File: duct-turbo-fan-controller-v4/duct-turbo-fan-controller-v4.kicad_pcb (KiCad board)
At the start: 2 copper layers, 42.7 x 48.8 mm, 45 parts, among them J1 Screw_Terminal_01x04, J2 Conn_01x04, J3 USB_OTG, J4 AudioJack4, J7 Conn_01x04, Q1 MMBT3904, Q2 BSS84, SW1 SW_Push, SW2 SW_Push, U1 SCD41-D-R2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

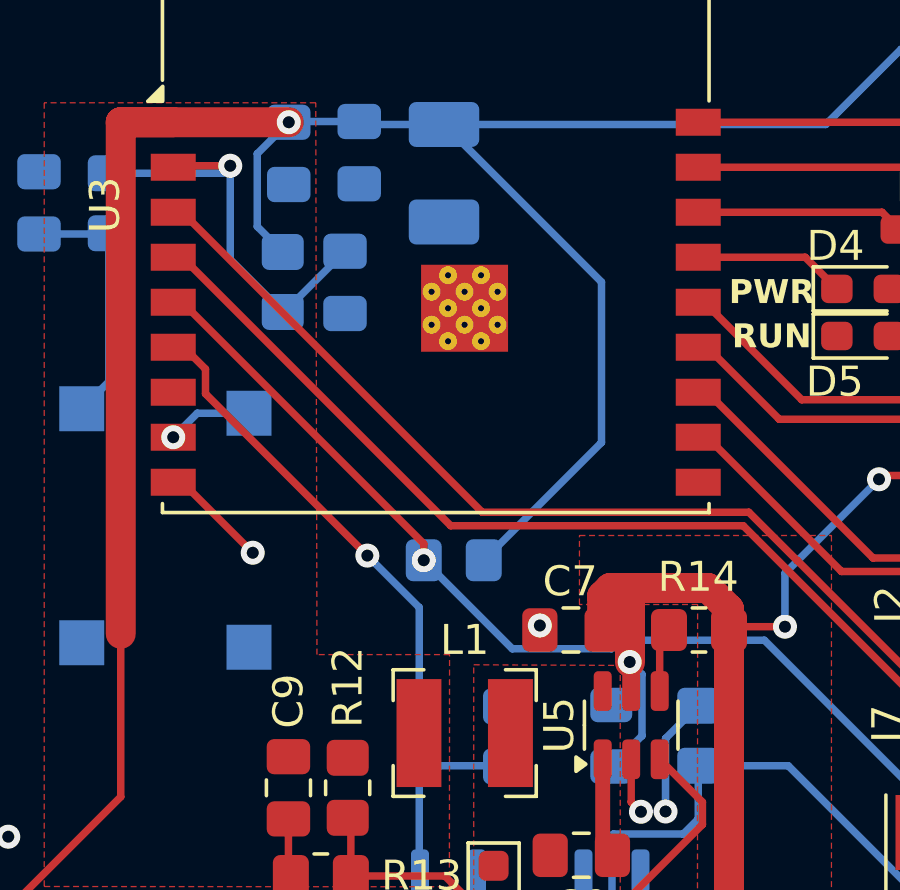
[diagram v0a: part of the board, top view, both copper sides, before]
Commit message: Add gnd tracks where fill zone incomplete.
Update leds in schematic to be more readable.
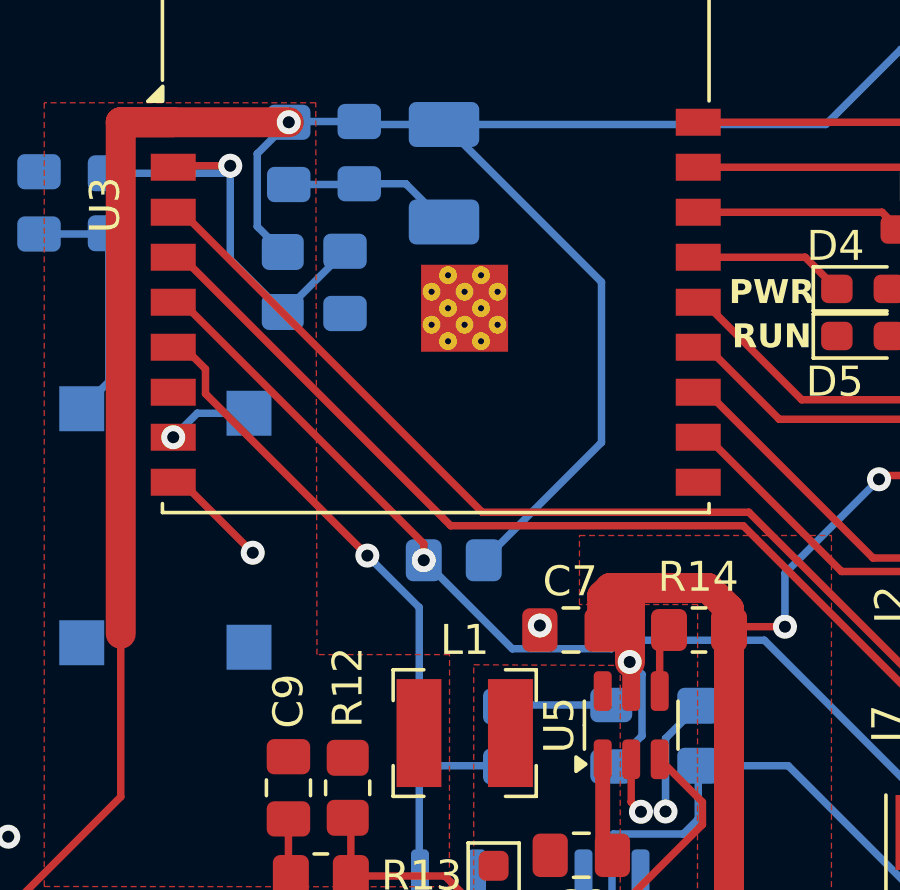
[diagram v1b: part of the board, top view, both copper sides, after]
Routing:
- net GND: track 37.1 -> 46.5 mm
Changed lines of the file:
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@@
+	)
+	(segment
+		(start 87.45 55.375)
+		(end 88.725 56.65)
+		(width 0.25)
+		(layer "B.Cu")
+		(net 2)
 	)
 	(segment
@@
 	)
 	(segment
+		(start 85.9 55.375)
+		(end 87.45 55.375)
+		(width 0.25)
+		(layer "B.Cu")
+		(net 2)
+	)
+	(segment
 		(start 89.825 78.3)
 		(end 89.825 80.055)
@@
 	)
 	(segment
+		(start 90.775 72.75)
+		(end 90.725 72.8)
+		(width 0.25)
+		(layer "B.Cu")
+		(net 2)
+	)
+	(segment
+		(start 83.55 55.4)
+		(end 85.875 55.4)
+		(width 0.25)
+		(layer "B.Cu")
+		(net 2)
+	)
+	(segment
 		(start 110.225 80.9)
 		(end 110.225 80.875)
+		(width 0.25)
+		(layer "B.Cu")
+		(net 2)
+	)
+	(segment
+		(start 85.875 55.4)
+		(end 85.9 55.375)
 		(width 0.25)
 		(layer "B.Cu")
@@
 		(width 0.25)
 		(layer "B.Cu")
+		(net 2)
+	)
+	(segment
+		(start 94.3 72.75)
+		(end 90.775 72.75)
+		(width 0.25)
+		(layer "B.Cu")

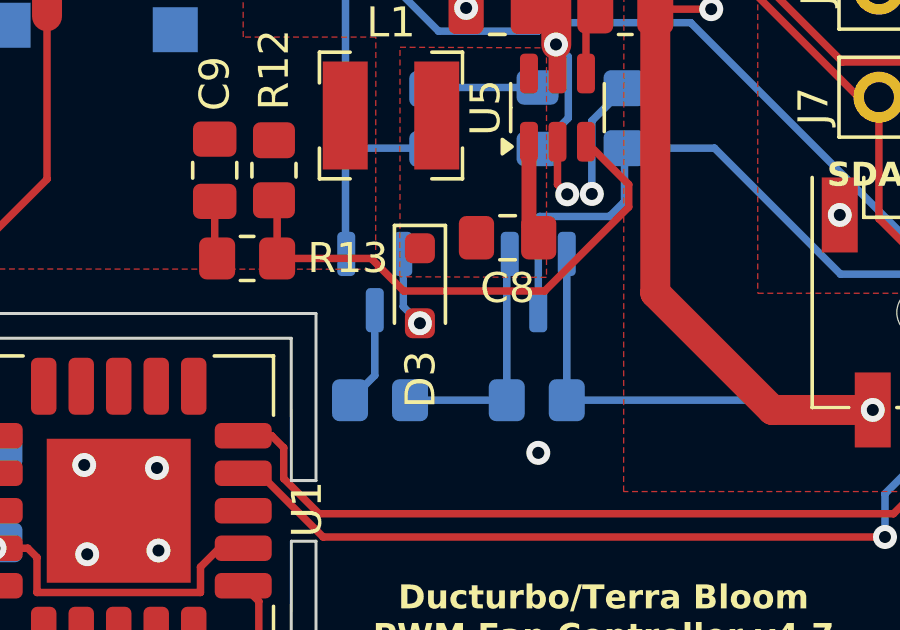
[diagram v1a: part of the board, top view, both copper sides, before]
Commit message: Fix buck diode footprint on pcb
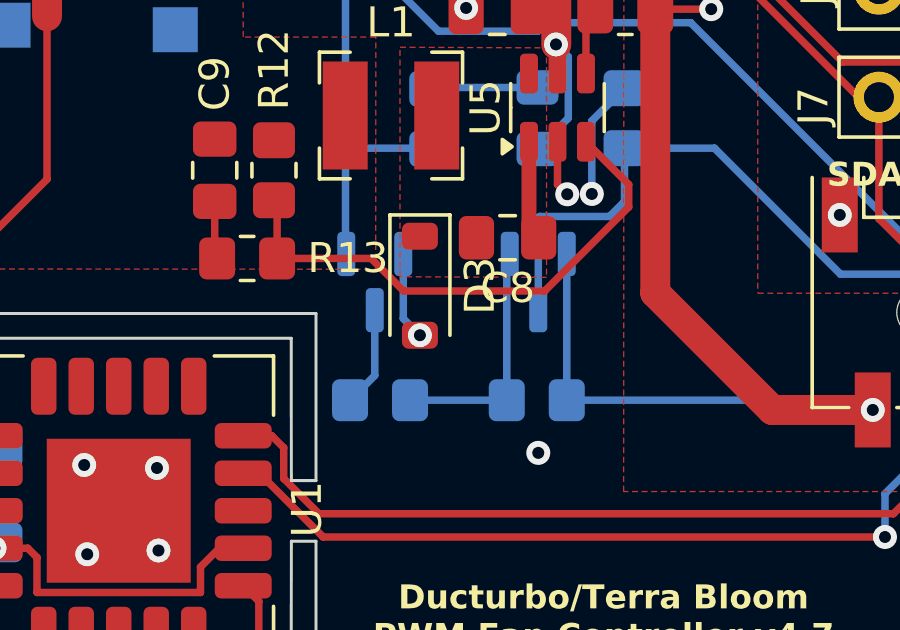
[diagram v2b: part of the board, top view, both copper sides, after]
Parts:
- C7, C9: value C_Small -> 10uF X7R
- C8: value C_Small -> 0.1uF
- D3: footprint Diode_SMD:D_SOD-323_HandSoldering -> Diode_SMD:D_SOD-123
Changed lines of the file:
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@@
 			)
 		)
-		(property "Value" "C_Small"
+		(property "Value" "0.1uF"
 			(at 0 1.68 0)
 			(layer "F.Fab")
@@
 			)
 		)
-		(property "Value" "C_Small"
+		(property "Value" "10uF X7R"
 			(at 0 1.68 90)
 			(layer "F.Fab")
@@
 		)
 	)
-	(footprint "Diode_SMD:D_SOD-323_HandSoldering"
+	(footprint "Diode_SMD:D_SOD-123"
 		(layer "F.Cu")
 		(at 90.38 79.36 -90)
-		(descr "SOD-323")
-		(tags "SOD-323")
+		(descr "SOD-123")
+		(tags "SOD-123")
 		(property "Reference" "D3"
-			(at 3.12 -0.02 90)
+			(at 0 -2 -90)
 			(layer "F.SilkS")
 			(effects
@@
 		)
 		(property "Value" "PMEG4005EGWX"
-			(at 0.1 1.9 90)
+			(at 0 2.1 -90)
 			(layer "F.Fab")
 			(effects
@@
 			)
 		)
-		(property "Footprint" "Diode_SMD:D_SOD-323_HandSoldering"
+		(property "Footprint" "Diode_SMD:D_SOD-123"
 			(at 0 0 -90)
 			(unlocked yes)
@@
 		(attr smd)
 		(fp_line
-			(start -2.01 0.85)
-			(end 1.25 0.85)
+			(start -2.36 1)
+			(end 1.65 1)
 			(stroke
 				(width 0.12)
@@
 		)
 		(fp_line
-			(start -2.01 -0.85)
-			(end -2.01 0.85)
+			(start -2.36 -1)
+			(end -2.36 1)
 			(stroke
 				(width 0.12)
@@
 		)
 		(fp_line
-			(start -2.01 -0.85)
-			(end 1.25 -0.85)
+			(start -2.36 -1)
+			(end 1.65 -1)
 			(stroke
 				(width 0.12)
@@
 		)
 		(fp_line
-			(start -2 0.95)
-			(end 2 0.95)
+			(start 2.35 1.15)
+			(end -2.35 1.15)
 			(stroke
 				(width 0.05)
@@
 		)
 		(fp_line
-			(start -2 -0.95)
-			(end -2 0.95)
+			(start -2.35 -1.15)
+			(end -2.35 1.15)
 			(stroke
 				(width 0.05)
@@
 		)
 		(fp_line
-			(start -2 -0.95)
-			(end 2 -0.95)
+			(start -2.35 -1.15)
+			(end 2.35 -1.15)
 			(stroke
 				(width 0.05)
@@
 		)
 		(fp_line
-			(start 2 -0.95)
-			(end 2 0.95)
+			(start 2.35 -1.15)
+			(end 2.35 1.15)
 			(stroke
 				(width 0.05)
@@
 		)
 		(fp_line
-			(start -0.9 0.7)
-			(end -0.9 -0.7)
+			(start -1.4 0.9)
+			(end -1.4 -0.9)
+			(stroke
+				(width 0.1)
+				(type solid)
+			)
+			(layer "F.Fab")
+		)
+		(fp_line
+			(start 1.4 0.9)
+			(end -1.4 0.9)
 			(stroke
 				(width 0.1)
@@
 		)
 		(fp_line
-			(start 0.9 0.7)
-			(end -0.9 0.7)
+			(start 0.25 0.4)
+			(end -0.35 0)
 			(stroke
 				(width 0.1)
@@
 		)
 		(fp_line
-			(start 0.2 0.35)
-			(end -0.3 0)
+			(start -0.75 0)
+			(end -0.35 0)
 			(stroke
 				(width 0.1)
@@
 		)
 		(fp_line
-			(start -0.3 0)
-			(end -0.5 0)
+			(start -0.35 0)
+			(end -0.35 0.55)
 			(stroke
 				(width 0.1)
@@
 		)
 		(fp_line
-			(start -0.3 0)
-			(end 0.2 -0.35)
+			(start -0.35 0)
+			(end 0.25 -0.4)
 			(stroke
 				(width 0.1)
@@
 		)
 		(fp_line
-			(start 0.2 0)
-			(end 0.45 0)
+			(start -0.35 0)
+			(end -0.35 -0.55)
 			(stroke
 				(width 0.1)
@@
 		)
 		(fp_line
-			(start -0.3 -0.35)
-			(end -0.3 0.35)
+			(start 0.25 0)
+			(end 0.75 0)
 			(stroke
 				(width 0.1)
@@
 		)
 		(fp_line
-			(start 0.2 -0.35)
-			(end 0.2 0.35)
+			(start 0.25 -0.4)
+			(end 0.25 0.4)
 			(stroke
 				(width 0.1)
@@
 		)
 		(fp_line
-			(start -0.9 -0.7)
-			(end 0.9 -0.7)
+			(start -1.4 -0.9)
+			(end 1.4 -0.9)
 			(stroke
 				(width 0.1)
@@
 		)
 		(fp_line
-			(start 0.9 -0.7)
-			(end 0.9 0.7)
+			(start 1.4 -0.9)
+			(end 1.4 0.9)
 			(stroke
 				(width 0.1)
@@
 		)
 		(fp_text user "${REFERENCE}"
-			(at 0 -1.85 90)
+			(at 0 -2 -90)
 			(layer "F.Fab")
 			(effects
@@
 		)
 		(pad "1" smd roundrect
-			(at -1.25 0 270)
-			(size 1 1)
+			(at -1.65 0 270)
+			(size 0.9 1.2)
 			(layers "F.Cu" "F.Paste" "F.Mask")
 			(roundrect_rratio 0.25)
@@
 		)
 		(pad "2" smd roundrect
-			(at 1.25 0 270)
-			(size 1 1)
+			(at 1.65 0 270)
+			(size 0.9 1.2)
 			(layers "F.Cu" "F.Paste" "F.Mask")
 			(roundrect_rratio 0.25)
@@
 			(pintype "passive")
 		)
-		(model "${KICAD8_3DMODEL_DIR}/Diode_SMD.3dshapes/D_SOD-323.wrl"
+		(model "${KICAD8_3DMODEL_DIR}/Diode_SMD.3dshapes/D_SOD-123.wrl"
 			(offset
 				(xyz 0 0 0)
@@
 			)
 		)
-		(property "Value" "C_Small"
+		(property "Value" "10uF X7R"
 			(at 0 1.68 0)
 			(layer "F.Fab")
@@
 	)
 	(via
-		(at 90.38 80.61)
+		(at 90.38 81.010004)
 		(size 0.8)
 		(drill 0.4)
@@
 	)
 	(segment
-		(start 89.825 80.055)
-		(end 90.38 80.61)
-		(width 0.25)
-		(layer "B.Cu")
-		(net 2)
-	)
-	(segment
 		(start 112.6 83.275)
 		(end 110.225 80.9)
@@
 	)
 	(segment
-		(start 89.825 78.3)
-		(end 89.825 80.055)
-		(width 0.25)
-		(layer "B.Cu")
-		(net 2)
-	)
-	(segment
 		(start 90.775 72.75)
 		(end 90.725 72.8)
@@
 	)
 	(segment
+		(start 89.825 78.3)
+		(end 89.825 80.455004)
+		(width 0.25)
+		(layer "B.Cu")
+		(net 2)
+	)
+	(segment
 		(start 111.2625 86.024327)
 		(end 111.025 86.261827)
 		(width 0.25)
 		(layer "B.Cu")
+		(net 2)
+	)
+	(segment
+		(start 89.825 80.455004)
+		(end 90.38 81.010004)
+		(width 0.25)
+		(layer "B.Cu")

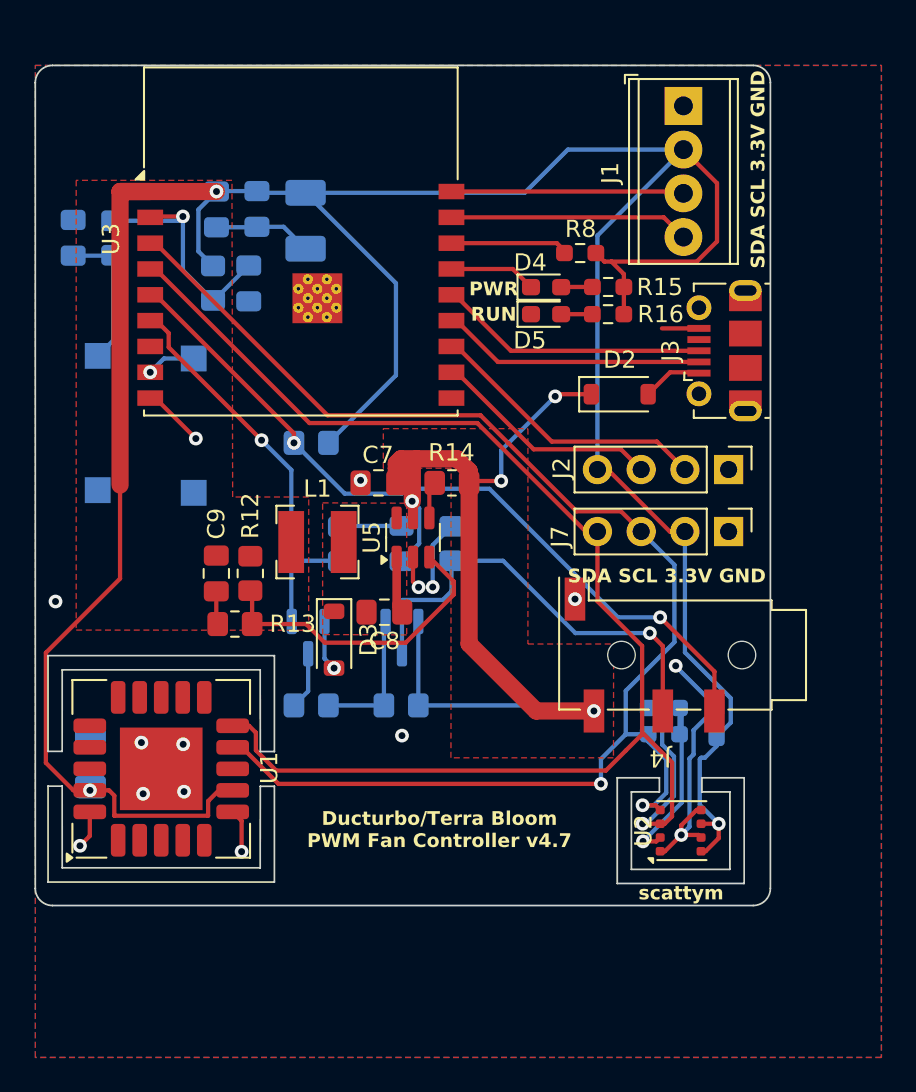
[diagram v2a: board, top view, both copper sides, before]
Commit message: Add input resistor from Tacho pin
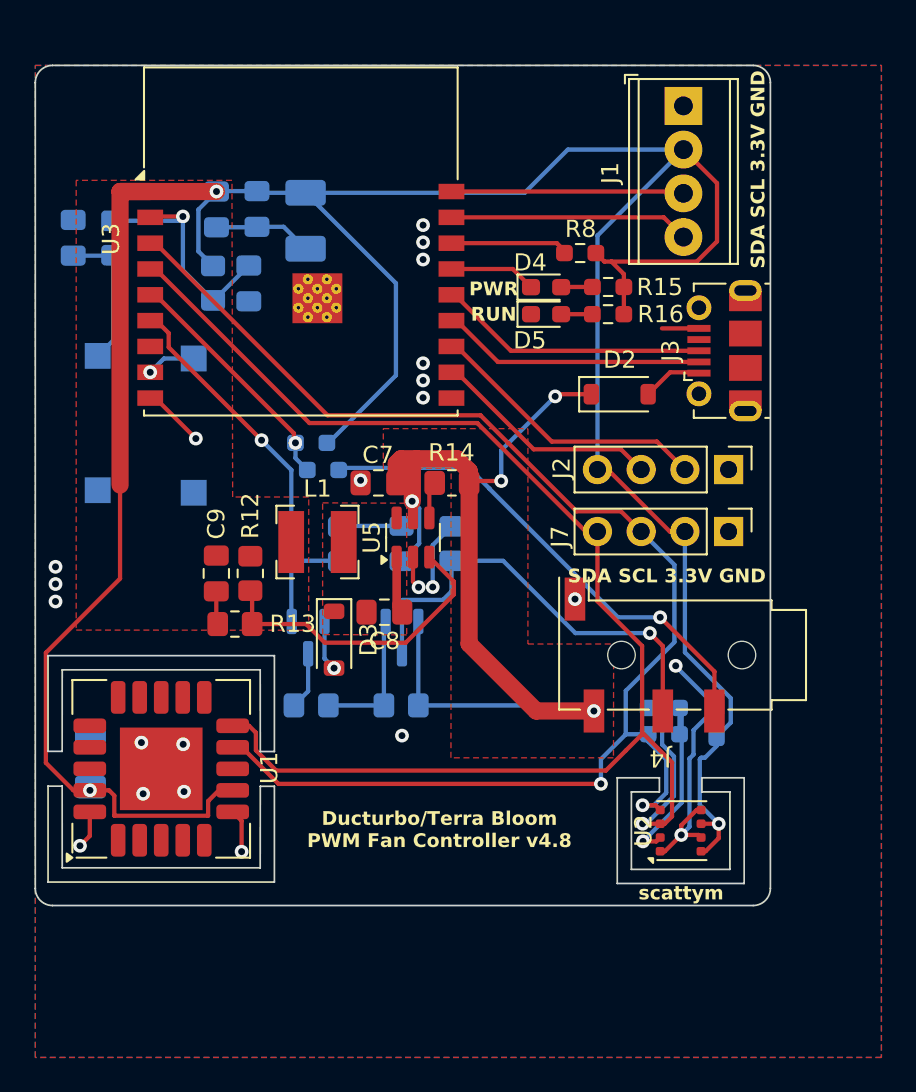
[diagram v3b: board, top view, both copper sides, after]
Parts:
- added R17: 100, Resistor_SMD:R_0603_1608Metric_Pad0.98x0.95mm_HandSolder, B.Cu at (89.7, 69.5)
- R6: footprint Resistor_SMD:R_0805_2012Metric_Pad1.20x1.40mm_HandSolder -> Resistor_SMD:R_0603_1608Metric_Pad0.98x0.95mm_HandSolder
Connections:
- J4 pad R2: Tacho -> Net-(J4-PadR2)
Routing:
- net Tacho: track 44.4 -> 13.8 mm, vias 2 -> 1
- net Net-(J4-PadR2): track 0.00 -> 29.1 mm, vias 0 -> 1
- net GND: vias 16 -> 24
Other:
- board text added: "Ducturbo/Terra Bloom PWM Fan Controller v4.8"
- board text removed: "Ducturbo/Terra Bloom PWM Fan Controller v4.7"

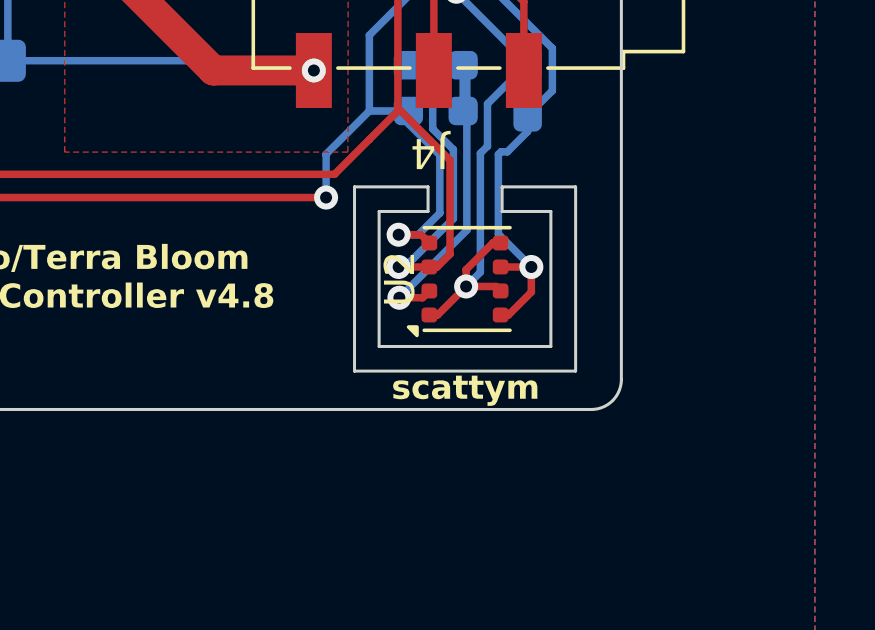
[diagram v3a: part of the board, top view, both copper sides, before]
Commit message: Fix bme688 wiring by adding +3.3V to CSB pin.
Was defaulting to spi mode and taking out the whole i2c link
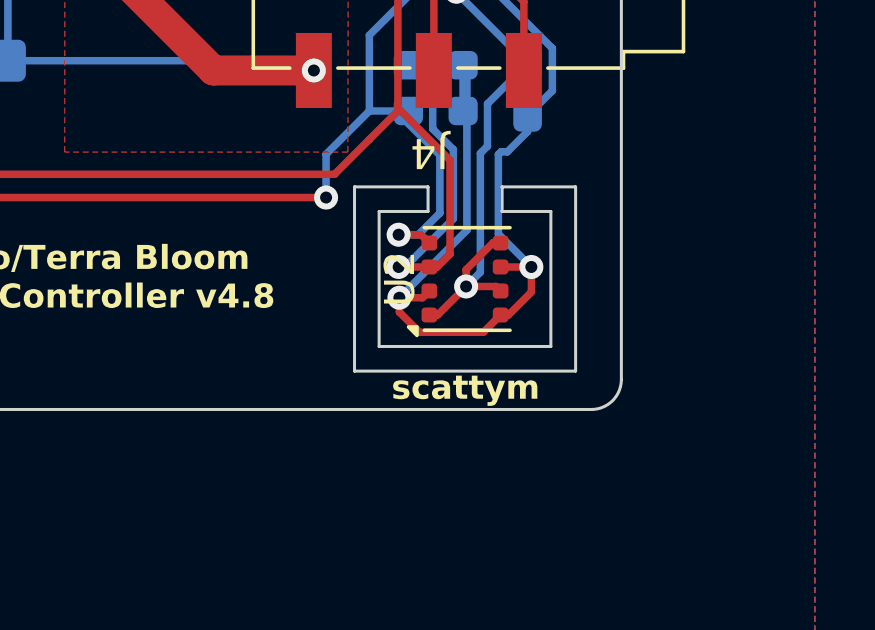
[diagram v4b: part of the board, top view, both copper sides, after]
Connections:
- R10 pad 2: Net-(U2-CSB) -> +3V3
- R11 pad 2: Net-(U2-CSB) -> +3V3
- U2 pad 2: Net-(U2-CSB) -> +3V3
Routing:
- net +3V3: track 177.2 -> 192.8 mm, vias 3 -> 4
- net Net-(U2-CSB): track 11.2 -> 0.00 mm, vias 1 -> 0
